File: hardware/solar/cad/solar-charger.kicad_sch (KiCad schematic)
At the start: 15 parts, among them J1 ISENSE_SOLAR, J2 Conn_01x02_Male, J3 ISENSE_DISCHARGE, J4 Conn_01x02_Male, Q1 AOI21357, Q2 AOI21357, Q3 AOI21357, Q4 AOI21357

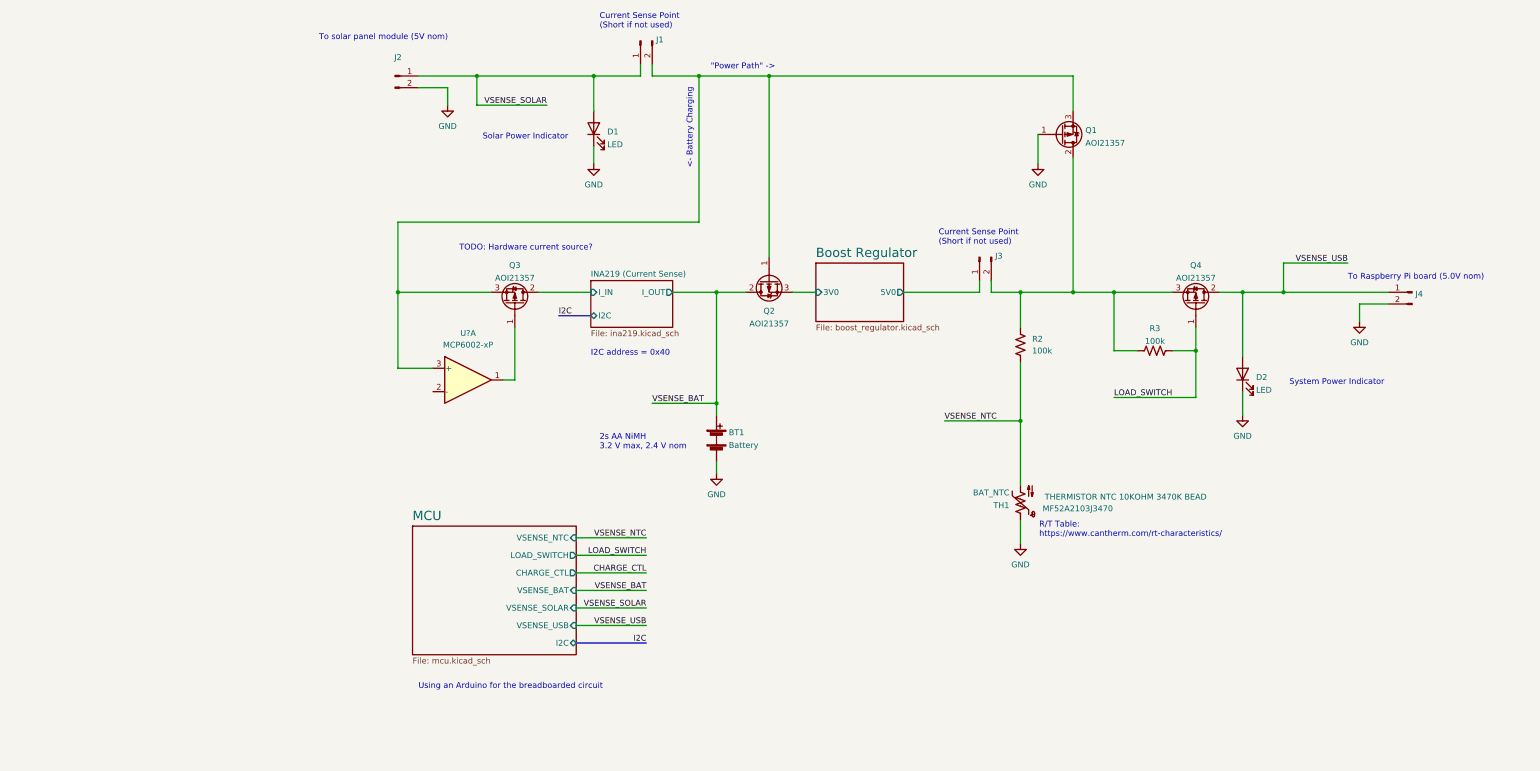
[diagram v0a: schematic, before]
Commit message: Attempt to roll our own charging but stop before I get carried away
This is actually a real pain in the ass, so we're not going to deal with
it yet. My thoughts are that we should focus on getting something out
the door otherwise I'm going to spend a long time designing a NiMH
charger.

Some problem/open questions in this design:
 - Constant current driver uses a lot of power if we want to support
   fast charging. ~3W of the 6W available.
 - Some kind of switching regulator would be more suited to the task I
   think. BQ24401 seems like a suitable part, relatively cheap.
 - Need an accurate (~1mV according to one source I read) voltage
   sensing circuit if we want to do ∆V/dt termination.

Saving this in this branch to inspire future improvements when we can
prove we need them.
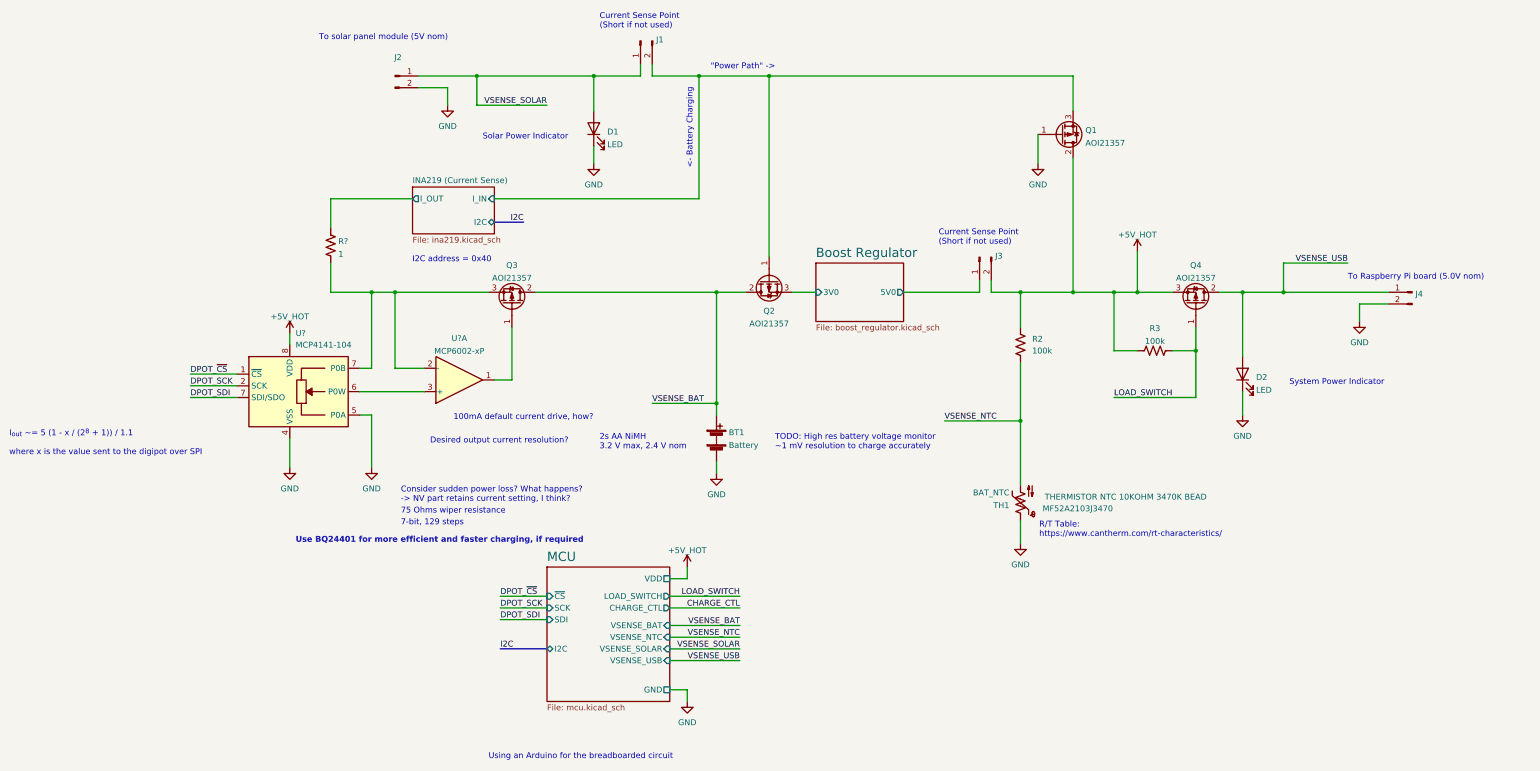
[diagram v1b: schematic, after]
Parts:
- added R?: 1, symbol Device:R_US
- added U?: MCP4141-104, Package_DIP:DIP-8_W7.62mm, symbol Potentiometer_Digital:MCP4141-104
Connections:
- net GND: now also U?.4 (VSS), U?.5 (P0A)
- net INA219 (Current Sense)/I_IN: now also J1.2 (Pin_2), Q1.3 (S), Q2.1 (G); no longer Q3.2 (D)
- net VSENSE_BAT: now also Q3.2 (D)
- net +5V: now reaches J3.2 (Pin_2), Q1.2 (D), Q4.3 (S), R2.1, R3.1
- net +5V: now also U?.8 (VDD)
- net at U?.2 (-): now also Q3.3 (S), R?.2, U?.7 (SDI/SDO)
- new net: U?.3 (+), U?.6 (P0W)
- new net DPOT_SCK: U?.2 (SCK)
- new net DPOT_SDI: U?.7 (SDI/SDO)
- new net DPOT_~{CS}: U?.1 (~{CS})
- new net INA219 (Current Sense)/I_OUT: R?.1
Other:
- sheet MCU ports: added GND, SCK, SDI, VDD, ~{CS}; removed none
- note added: "100mA default current drive, how?"
- note added: "7-bit, 129 steps"
- note added: "75 Ohms wiper resistance"
- note added: "Consider sudden power loss? What happens? -> NV part retains current setting, I think?"
- note added: "Desired output current resolution?"
- note added: "I_{out} ~= 5 (1 - x / (2^{8} + 1)) / 1.1 where x is the value sent to the digipot over SPI"
- note added: "TODO: High res battery voltage monitor ~1 mV resolution to charge accurately"
- note added: "Use BQ24401 for more efficient and faster charging, if required"
- note removed: "TODO: Hardware current source?"
- moved on the sheet: Q3, U?A
